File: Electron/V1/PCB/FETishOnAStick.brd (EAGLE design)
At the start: 89.5 x 29.3 mm, 18 parts, among them Q1 FDD8780 or FDD8451, Q2 BSS138 - 200mA/50V, Q3 FDD8780 or FDD8451

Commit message: Initial version.
NB: Missing track for A4.
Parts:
- R1, R7, R8: value 0R -> 10R
- R2, R6, R9: value 0R -> 10k
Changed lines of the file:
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@@
 <grid distance="0.05" unitdist="inch" unit="inch" style="lines" multiple="1" display="yes" altdistance="0.0125" altunitdist="inch" altunit="inch"/>
 <layers>
-<layer number="1" name="Top" color="4" fill="1" visible="yes" active="yes"/>
+<layer number="1" name="Top" color="4" fill="1" visible="no" active="yes"/>
 <layer number="2" name="Route2" color="1" fill="3" visible="no" active="no"/>
 <layer number="3" name="Route3" color="4" fill="3" visible="no" active="no"/>
@@
 <attribute name="NAME" x="81.407" y="17.9705" size="0.8128" layer="25"/>
 </element>
-<element name="R6" library="SparkFun-Resistors" package="0805" value="0R" x="78.105" y="12.3825" smashed="yes" rot="R90">
+<element name="R6" library="SparkFun-Resistors" package="0805" value="10k" x="78.105" y="12.3825" smashed="yes" rot="R90">
 <attribute name="NAME" x="78.5495" y="15.0495" size="0.8128" layer="25" rot="R180"/>
 </element>
-<element name="R7" library="SparkFun-Resistors" package="0805" value="0R" x="73.9775" y="19.05" smashed="yes" rot="R180">
+<element name="R7" library="SparkFun-Resistors" package="0805" value="10R" x="73.9775" y="19.05" smashed="yes" rot="R180">
 <attribute name="NAME" x="73.787" y="20.7645" size="0.8128" layer="25" rot="R180"/>
 </element>
-<element name="R8" library="SparkFun-Resistors" package="0805" value="0R" x="73.9775" y="21.9075" smashed="yes" rot="R180">
+<element name="R8" library="SparkFun-Resistors" package="0805" value="10R" x="73.9775" y="21.9075" smashed="yes" rot="R180">
 <attribute name="NAME" x="72.5805" y="23.0505" size="0.8128" layer="25"/>
 </element>
-<element name="R9" library="SparkFun-Resistors" package="0805" value="0R" x="78.74" y="21.9075" smashed="yes">
+<element name="R9" library="SparkFun-Resistors" package="0805" value="10k" x="78.74" y="21.9075" smashed="yes">
 <attribute name="NAME" x="80.518" y="21.463" size="0.8128" layer="25"/>
 </element>
@@
 <attribute name="NAME" x="81.7055" y="3.3655" size="0.8128" layer="25"/>
 </element>
-<element name="R1" library="SparkFun-Resistors" package="0805" value="0R" x="72.39" y="1.27" smashed="yes" rot="R180">
+<element name="R1" library="SparkFun-Resistors" package="0805" value="10R" x="72.39" y="1.27" smashed="yes" rot="R180">
 <attribute name="NAME" x="72.1995" y="2.9845" size="0.8128" layer="25" rot="R180"/>
 </element>
-<element name="R2" library="SparkFun-Resistors" package="0805" value="0R" x="77.47" y="1.27" smashed="yes" rot="R180">
+<element name="R2" library="SparkFun-Resistors" package="0805" value="10k" x="77.47" y="1.27" smashed="yes" rot="R180">
 <attribute name="NAME" x="78.867" y="2.9845" size="0.8128" layer="25" rot="R180"/>
 </element>

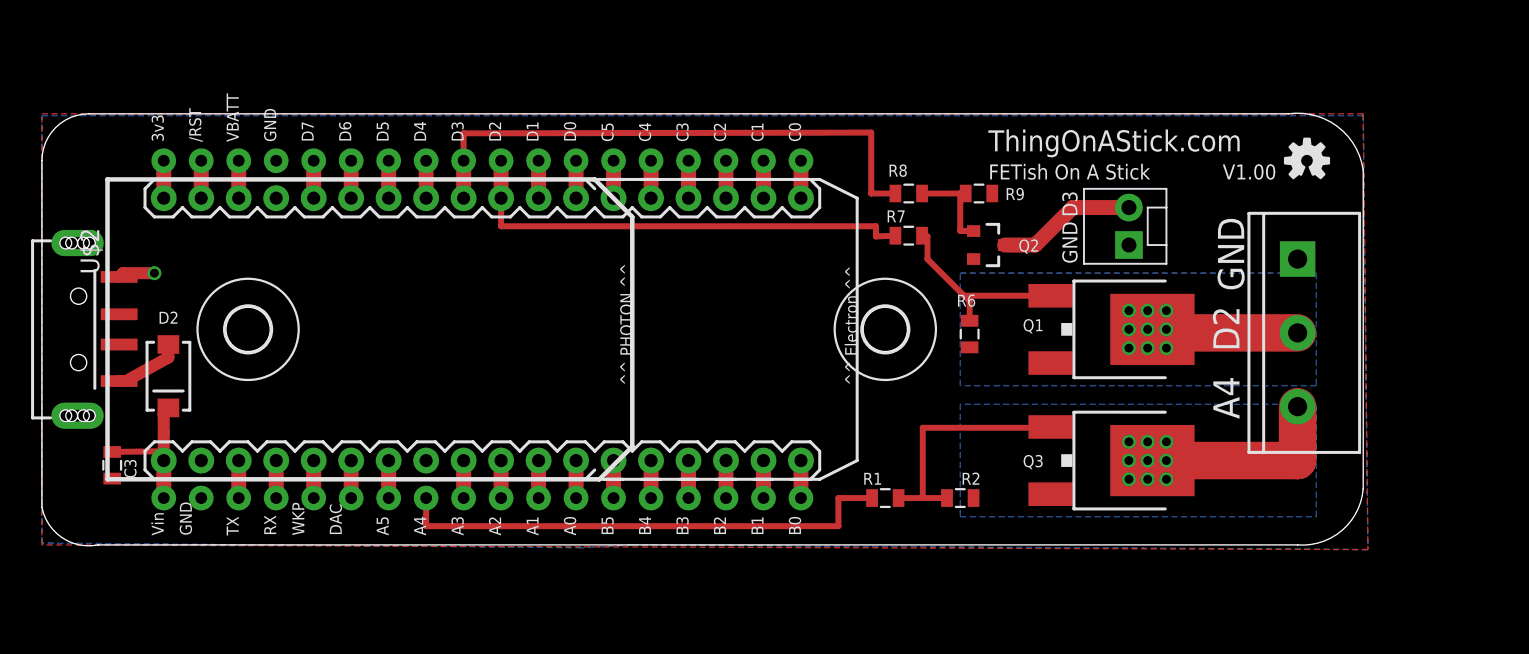
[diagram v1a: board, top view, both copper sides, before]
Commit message: Updated identifiers, tidied up and added BOMs and images
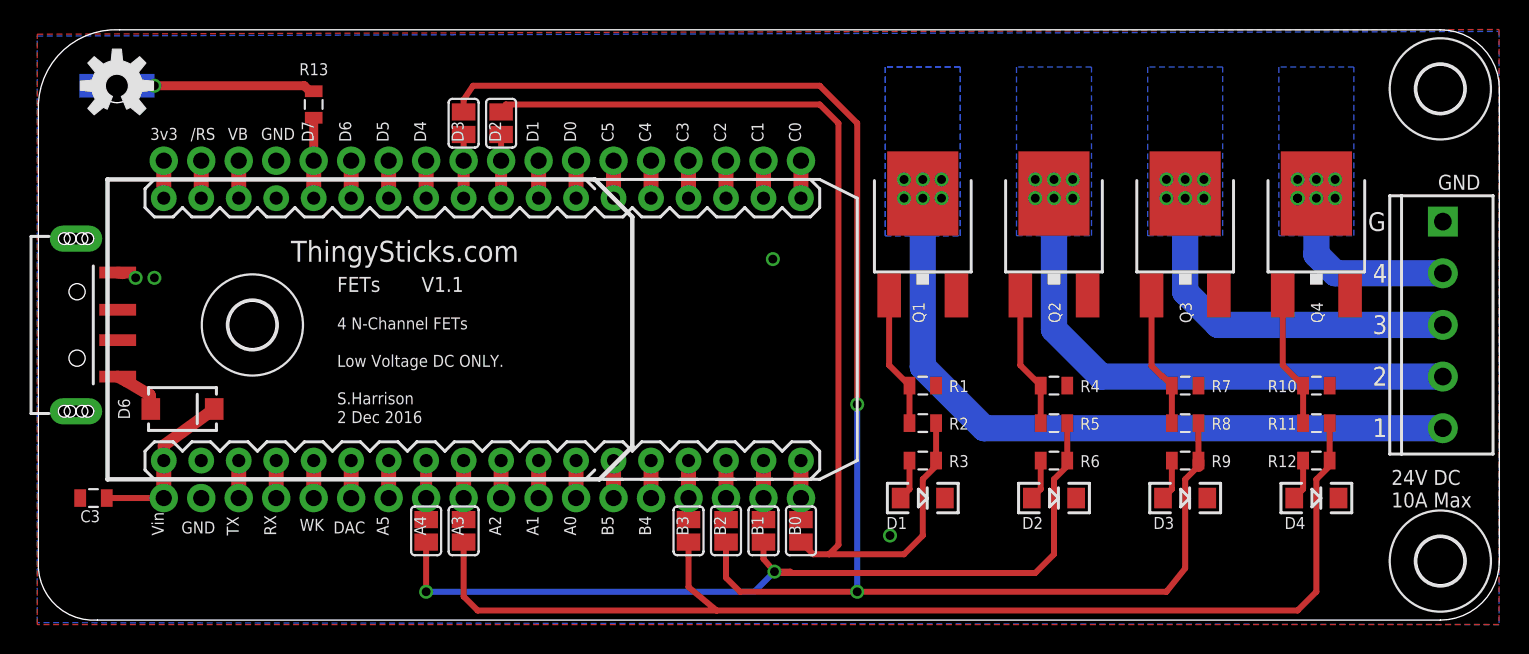
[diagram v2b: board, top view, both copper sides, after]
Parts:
- removed H2: MOUNT-HOLE3.0, holes:3,0
- removed JP2: (no value), SparkFun-Connectors:MOLEX-1X2
- removed LOGO2: OSHW-LOGOS, SparkFun-Aesthetics:OSHW-LOGO-S
- added D1, D3, D4: BLUE, SparkFun-LED:LED-1206
- added D5: (no value), SparkFun-LED:LED-1206-BOTTOM
- added D6: (no value), SparkFun-DiscreteSemi:SMA-DIODE
- added H3, H4: MOUNT-HOLE3.2, holes:3,2
- added LOGO1: OSHW-LOGOM, SparkFun-Aesthetics:OSHW-LOGO-M
- added Q4: FDD8780 or FDD8451, SparkFun-DiscreteSemi:DPAK
- added R10, R4: 10k, SparkFun-Resistors:0805
- added R11, R5: 10R, SparkFun-Resistors:0805
- added R12, R13, R3: 1k5, SparkFun-Resistors:0805
- added SJ1, SJ2, SJ3, SJ4, SJ5, SJ6, SJ7, SJ8: (no value), jumper:SJ
- D2: value (none) -> BLUE; device SparkFun-DiscreteSemi:SMA-DIODE -> SparkFun-LED:LED-1206
- H1: value MOUNT-HOLE3.0 -> MOUNT-HOLE3.2; device holes:3,0 -> holes:3,2
- JP1: device SparkFun-Connectors:SCREWTERMINAL-5MM-3 -> SparkFun-Connectors:SCREWTERMINAL-3.5MM-5
- Q2: value BSS138 - 200mA/50V -> FDD8780 or FDD8451; device SparkFun-DiscreteSemi:SOT23-3 -> SparkFun-DiscreteSemi:DPAK
- R1, R7: value 10R -> 10k
- R2: value 10k -> 10R
- R6, R9: value 10k -> 1k5
- moved D2 60.6 mm to (83.8, 1.27), turned to 0 degrees
- moved R8 24.4 mm to (92.7, 6.35), turned to 0 degrees
- moved R9 22.9 mm to (92.7, 3.81), turned to 180 degrees
- moved R7 21.3 mm to (92.7, 8.89)
- moved Q3 16.9 mm to (92.7, 20.3), turned to 0 degrees
- moved Q1 15.9 mm to (74.9, 20.3), turned to 0 degrees
- moved R6 10.3 mm to (83.8, 3.81), turned to 180 degrees
- moved JP1 10.2 mm to (110.2, 20.0)
- moved R1 8.03 mm to (74.9, 8.89)
- moved R2 5.68 mm to (74.9, 6.35), turned to 0 degrees
- moved Q2 4.84 mm to (83.8, 20.3), turned to 0 degrees
- moved C3 2.56 mm to (18.7, 1.27), turned to 0 degrees
- moved H1 0.42 mm to (29.5, 13.0)
- moved CONN1 0.32 mm to (14.5, 13.0)
- renumbered U$2 to U2
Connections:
- removed net N$3: Q3.1, R1.1, R2.2
- removed net SMALL_FET: R8.2, U2.D3, U2.D3_1
- removed net SMALL_FET_RETURN: JP2.2, Q2.3
- new net BIG_FET_3: R8.2, R9.1, SJ2.1, SJ6.2
- new net BIG_FET_3_RETURN: JP1.3, Q3.4
- new net BIG_FET_4: R11.2, R12.1, SJ1.1, SJ7.1
- new net BIG_FET_4_RETURN: JP1.2, Q4.4
- new net D7: R13.1, U2.D7, U2.D7_1
- new net N$105: Q2.1, R4.2, R5.1
- new net N$12: D2.A, R6.2
- new net N$19: D5.A, R13.2
- new net N$21: Q3.1, R7.2, R8.1
- new net N$22: D3.A, R9.2
- new net N$30: SJ8.2, U2.A4, U2.A4_1
- new net N$4: Q4.1, R10.2, R11.1
- new net N$43: SJ6.1, U2.D3, U2.D3_1
- new net N$49: SJ5.1, U2.D2, U2.D2_1
- net 5V: now also D6.C; no longer D2.C
- net BIG_FET_1: now also R2.2, R3.1, SJ4.1, SJ5.2; no longer R7.2, U2.D2, U2.D2_1
- net BIG_FET_1_RETURN: now also JP1.5; no longer JP1.2
- net BIG_FET_2: now also R5.2, R6.1, SJ3.1, SJ8.1; no longer R1.2, U2.A4, U2.A4_1
- net BIG_FET_2_RETURN: now also JP1.4, Q2.4; no longer JP1.3, Q3.4
- net GND: now also D1.C, D2.C, D3.C, D4.C, D5.C, Q2.3, Q4.3, R1.1, R10.1, R4.1, R7.1; no longer JP2.1, Q2.2, R2.1, R6.1, R9.2
- net N$1: now also D6.A; no longer D2.A
- net N$11: now also D1.A, R3.2; no longer U2.D7, U2.D7_1
- net N$13: now also D4.A, R12.2; no longer Q2.1, R8.1, R9.1
- net N$27: now also R1.2, R2.1; no longer R6.2, R7.1
- net N$31: now also SJ4.2
- net N$33: now also SJ3.2
- net N$35: now also SJ2.2
- net N$36: now also SJ1.2
- net N$42: now also SJ7.2
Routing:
- net BIG_FET_3: track 0.00 -> 105.7 mm, vias 0 -> 2
- net BIG_FET_4: track 0.00 -> 79.7 mm
- net BIG_FET_1_RETURN: track 10.1 -> 50.6 mm, vias 9 -> 6
- net BIG_FET_1: track 31.9 -> 70.6 mm
- net SMALL_FET: track 37.8 -> 0.00 mm
- net BIG_FET_3_RETURN: track 0.00 -> 27.0 mm, vias 0 -> 6
- net BIG_FET_2: track 34.0 -> 59.8 mm, vias 0 -> 2
- net BIG_FET_2_RETURN: track 13.5 -> 39.1 mm, vias 9 -> 6
- net N$3: track 16.8 -> 0.00 mm
- net BIG_FET_4_RETURN: track 0.00 -> 15.1 mm, vias 0 -> 7
- net N$19: track 0.00 -> 11.7 mm, vias 0 -> 1
- net SMALL_FET_RETURN: track 9.48 -> 0.00 mm
- net N$21: track 0.00 -> 9.26 mm
- net N$4: track 0.00 -> 9.23 mm
- net N$105: track 0.00 -> 9.23 mm
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- added copper zone on layer 16, net BIG_FET_3_RETURN
- added copper zone on layer 16, net BIG_FET_4_RETURN
- added copper zone on layer 16, net N$50
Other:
- board size 89.5 x 29.3 mm -> 99 x 40 mm
- board text added: "1"
- board text added: "2"
- board text added: "2 Dec 2016"
- board text added: "24V DC 10A Max"
- board text added: "3"
- board text added: "4"
- board text added: "4 N-Channel FETs"
- board text added: "FETs"
- board text added: "G"
- board text added: "Low Voltage DC ONLY."
- board text added: "S.Harrison"
- board text added: "ThingySticks.com"
- board text added: "V1.1"
- board text removed: "A4"
- board text removed: "D2"
- board text removed: "D3"
- board text removed: "FETish On A Stick"
- board text removed: "ThingOnAStick.com"
- board text removed: "V1.00"
- board text removed: "^^ Electron ^^"
- board text removed: "^^ PHOTON ^^"
